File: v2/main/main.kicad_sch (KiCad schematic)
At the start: 90 parts, among them SW1 SW_PUSH, SW10 SW_PUSH, SW11 SW_PUSH, SW12 SW_PUSH, SW13 SW_PUSH, SW14 SW_PUSH, SW15 SW_PUSH, SW16 SW_PUSH, SW17 SW_PUSH, SW18 SW_PUSH, SW19 SW_PUSH, SW2 SW_PUSH, SW20 SW_PUSH, SW21 SW_PUSH, SW22 SW_PUSH, SW23 SW_PUSH, SW24 SW_PUSH, SW25 SW_PUSH, SW26 SW_PUSH, SW27 SW_PUSH, SW28 SW_PUSH, SW29 SW_PUSH, SW3 SW_PUSH, SW30 SW_PUSH, SW31 SW_PUSH, SW32 SW_PUSH, SW33 SW_PUSH, SW34 SW_PUSH, SW35 SW_PUSH, SW36 SW_PUSH, SW37 SW_PUSH, SW38 SW_PUSH, SW39 SW_PUSH, SW4 SW_PUSH, SW40 SW_PUSH, SW41 SW_PUSH, SW42 SW_PUSH, SW43 SW_PUSH, SW44 SW_PUSH, SW45 SW_PUSH, SW5 SW_PUSH, SW6 SW_PUSH, SW7 SW_PUSH, SW8 SW_PUSH, SW9 SW_PUSH

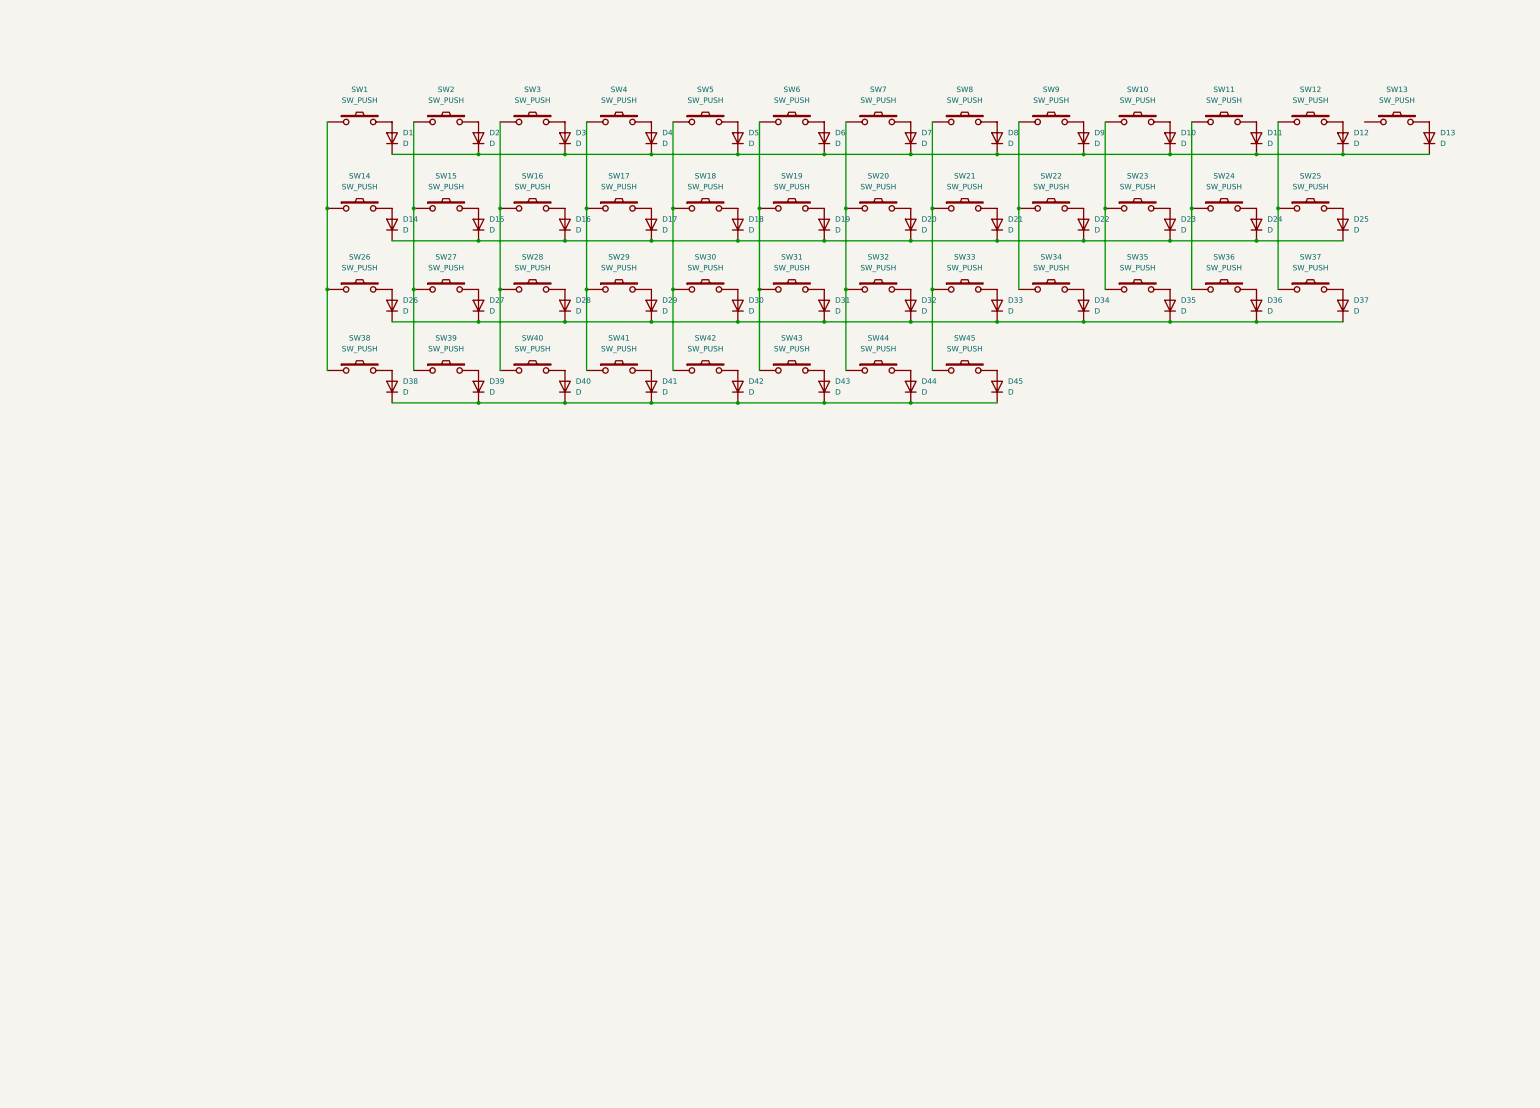
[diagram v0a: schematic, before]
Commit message: Add initial KiCad project files for version 2
- Created top.kicad_pro with board design settings, rules, and dimensions.
- Added top.kicad_sch with basic schematic structure and metadata.
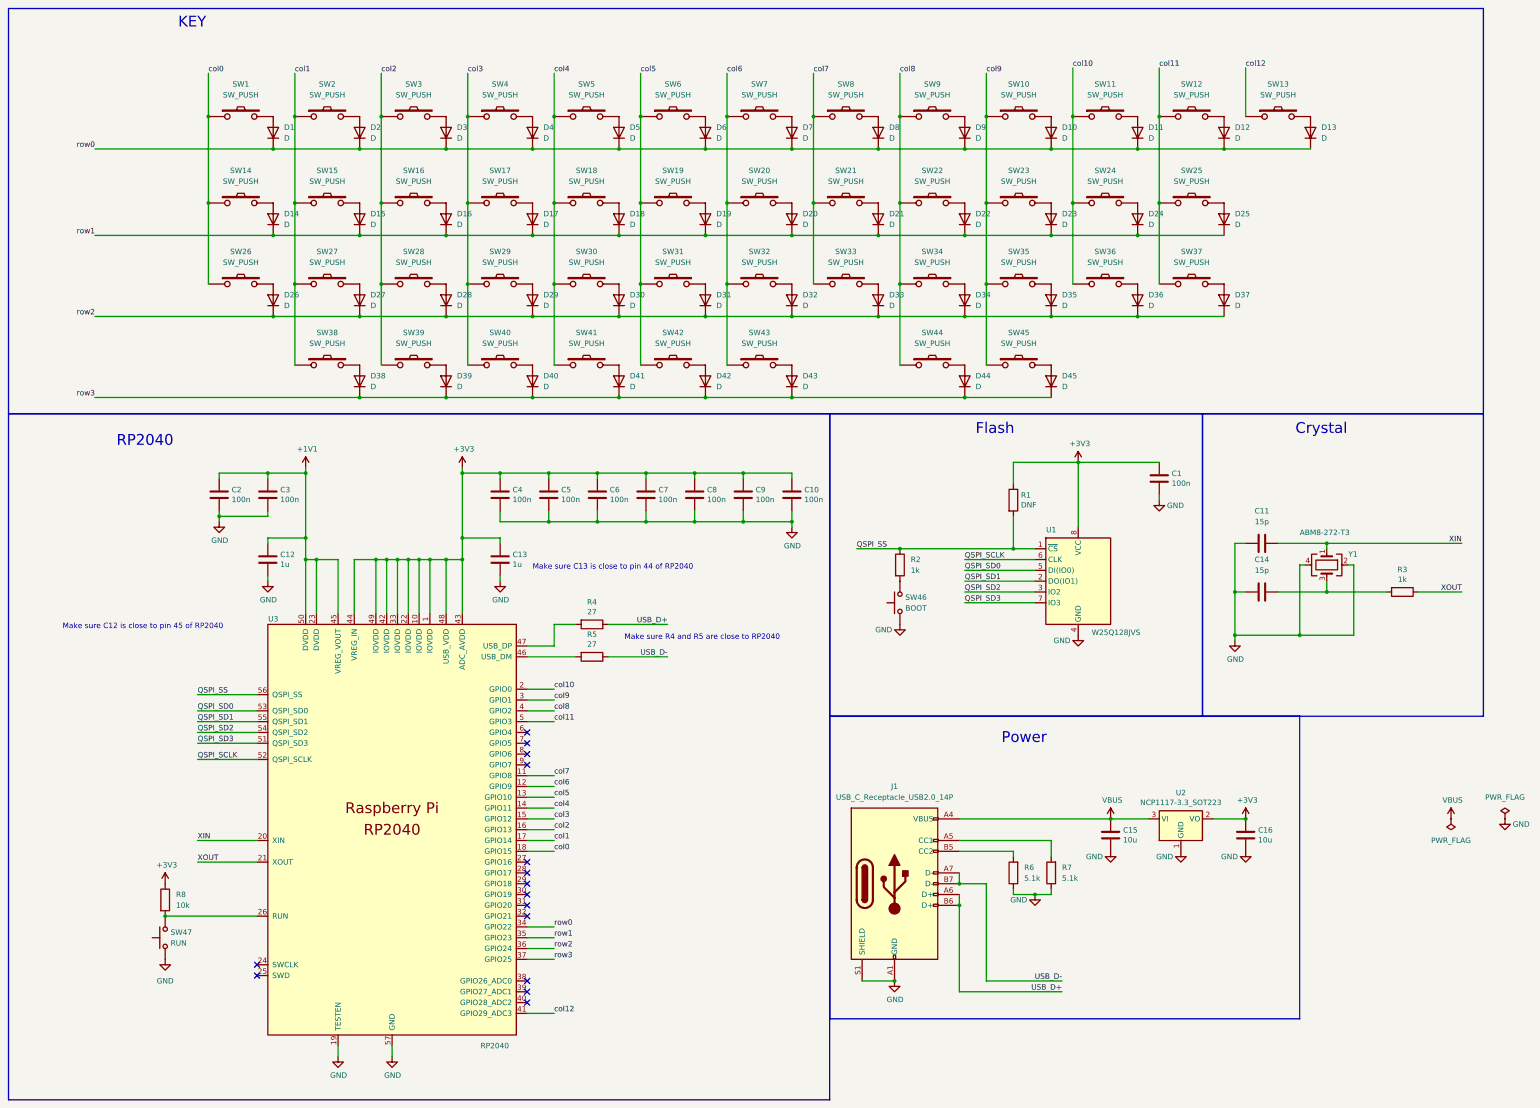
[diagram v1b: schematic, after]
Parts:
- added C1, C10, C2, C3, C4, C5, C6, C7, C8, C9: 100n, Capacitor_SMD:C_0402_1005Metric, symbol Device:C
- added C11, C14: 15p, Capacitor_SMD:C_0603_1608Metric, symbol Device:C
- added C12, C13: 1u, Capacitor_SMD:C_0402_1005Metric, symbol Device:C
- added C15, C16: 10u, Capacitor_SMD:C_0805_2012Metric, symbol Device:C
- added J1: USB_C_Receptacle_USB2.0_14P, Connector_USB:USB_C_Receptacle_Palconn_UTC16-G, symbol Connector:USB_C_Receptacle_USB2.0_14P
- added R1: DNF, Resistor_SMD:R_0402_1005Metric, symbol Device:R
- added R2, R3: 1k, Resistor_SMD:R_0402_1005Metric, symbol Device:R
- added R4, R5: 27, Resistor_SMD:R_0603_1608Metric, symbol Device:R
- added R6, R7: 5.1k, Resistor_SMD:R_0402_1005Metric, symbol Device:R
- added R8: 10k, Resistor_SMD:R_0402_1005Metric, symbol Device:R
- added SW46: BOOT, kamo3_footprint:Tact_Switch_5.1_5.1mm_SMD, symbol kamo3_symbol:SW_Push_4pin
- added SW47: RUN, kamo3_footprint:Tact_Switch_5.1_5.1mm_SMD, symbol kamo3_symbol:SW_Push_4pin
- added U1: W25Q128JVS, Package_SO:SOIC-8_5.23x5.23mm_P1.27mm, symbol Memory_Flash:W25Q128JVS
- added U2: NCP1117-3.3_SOT223, Package_TO_SOT_SMD:SOT-223-3_TabPin2, symbol Regulator_Linear:NCP1117-3.3_SOT223
- added U3: RP2040, rp2040:RP2040-QFN-56, symbol rp2040:RP2040
- added Y1: ABM8-272-T3, Crystal:Crystal_SMD_3225-4Pin_3.2x2.5mm, symbol Device:Crystal_GND24
- D1, D10, D11, D12, D13, D14, D15, D16, D17, D18, D19, D2, D20, D21, D22, D23, D24, D25, D26, D27, D28, D29, D3, D30, D31, D32, D33, D34, D35, D36, D37, D38, D39, D4, D40, D41, D42, D43, D44, D45, D5, D6, D7, D8, D9: LCSC (none) -> C8598
- SW41: footprint kamo3_footprint:SW_CherryMX_Hotswap_2.25u -> kamo3_footprint:SW_CherryMX_Hotswap_1.00u
- SW42: footprint kamo3_footprint:SW_CherryMX_Hotswap_2.75u -> kamo3_footprint:SW_CherryMX_Hotswap_1.00u
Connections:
- net col11: now reaches SW12.1, SW25.1, SW37.1
- net col11: now also U3.5 (GPIO3)
- net row1: now reaches D14.1 (K), D15.1 (K), D16.1 (K), D17.1 (K), D18.1 (K), D19.1 (K), D20.1 (K), D21.1 (K), D22.1 (K), D23.1 (K), D24.1 (K), D25.1 (K)
- net row1: now also U3.35 (GPIO23)
- net row3: now reaches D38.1 (K), D39.1 (K), D40.1 (K), D41.1 (K), D42.1 (K), D43.1 (K), D44.1 (K), D45.1 (K)
- net row3: now also U3.37 (GPIO25)
- net col1: now reaches SW15.1, SW2.1, SW27.1
- net col1: now also SW38.1, U3.17 (GPIO14); no longer SW39.1
- net col5: now reaches SW19.1, SW31.1, SW6.1
- net col5: now also SW42.1, U3.13 (GPIO10); no longer SW43.1
- net col6: now reaches SW20.1, SW32.1, SW7.1
- net col6: now also SW43.1, U3.12 (GPIO9); no longer SW44.1
- net row2: now reaches D26.1 (K), D27.1 (K), D28.1 (K), D29.1 (K), D30.1 (K), D31.1 (K), D32.1 (K), D33.1 (K), D34.1 (K), D35.1 (K), D36.1 (K), D37.1 (K)
- net row2: now also U3.36 (GPIO24)
- net col4: now reaches SW18.1, SW30.1, SW5.1
- net col4: now also SW41.1, U3.14 (GPIO11); no longer SW42.1
- net row0: now reaches D1.1 (K), D10.1 (K), D11.1 (K), D12.1 (K), D13.1 (K), D2.1 (K), D3.1 (K), D4.1 (K), D5.1 (K), D6.1 (K), D7.1 (K), D8.1 (K), D9.1 (K)
- net row0: now also U3.34 (GPIO22)
- net col2: now reaches SW16.1, SW28.1, SW3.1
- net col2: now also SW39.1, U3.16 (GPIO13); no longer SW40.1
- net col3: now reaches SW17.1, SW29.1, SW4.1
- net col3: now also SW40.1, U3.15 (GPIO12); no longer SW41.1
- net col0: now reaches SW1.1, SW14.1, SW26.1
- net col0: now also U3.18 (GPIO15); no longer SW38.1
- net col9: now reaches SW10.1, SW23.1, SW35.1
- net col9: now also SW45.1, U3.3 (GPIO1)
- net col8: now reaches SW22.1, SW34.1, SW9.1
- net col8: now also SW44.1, U3.4 (GPIO2)
- net col7: now reaches SW21.1, SW33.1, SW8.1
- net col7: now also U3.11 (GPIO8); no longer SW45.1
- net col10: now reaches SW11.1, SW24.1, SW36.1
- net col10: now also U3.2 (GPIO0)
- net col12: now reaches SW13.1
- net col12: now also U3.41 (GPIO29_ADC3)
- new net: C14.2, R3.2, Y1.3
- new net: R5.2, U3.46 (USB_DM)
- new net: R8.2, SW47.3, SW47.4, U3.26 (RUN)
- new net: J1.B5 (CC2), R6.2
- new net: R2.2, SW46.3, SW46.4
- new net: R4.2, U3.47 (USB_DP)
- new net: J1.A5 (CC1), R7.2
- new net +1V1: C12.1, C2.1, C3.1, U3.23 (DVDD), U3.45 (VREG_VOUT), U3.50 (DVDD)
- new net +3V3: C1.1, C10.1, C13.1, C16.1, C4.1, C5.1, C6.1, C7.1, C8.1, C9.1, R1.1, R8.1, U1.8 (VCC), U2.2 (VO), U3.1 (IOVDD), U3.10 (IOVDD), U3.22 (IOVDD), U3.33 (IOVDD), U3.42 (IOVDD), U3.43 (ADC_AVDD), U3.44 (VREG_IN), U3.48 (USB_VDD), U3.49 (IOVDD)
- new net GND: C1.2, C10.2, C11.1, C12.2, C13.2, C14.1, C15.2, C16.2, C2.2, C3.2, C4.2, C5.2, C6.2, C7.2, C8.2, C9.2, J1.A1 (GND), J1.A12 (GND), J1.B1 (GND), J1.B12 (GND), J1.S1 (SHIELD), R6.1, R7.1, SW46.1, SW46.2, SW47.1, SW47.2, U1.4 (GND), U2.1 (GND), U3.19 (TESTEN), U3.57 (GND), Y1.2, Y1.4
- new net QSPI_SCLK: U1.6 (CLK), U3.52 (QSPI_SCLK)
- new net QSPI_SD0: U1.5 (DI(IO0)), U3.53 (QSPI_SD0)
- new net QSPI_SD1: U1.2 (DO(IO1)), U3.55 (QSPI_SD1)
- new net QSPI_SD2: U1.3 (IO2), U3.54 (QSPI_SD2)
- new net QSPI_SD3: U1.7 (IO3), U3.51 (QSPI_SD3)
- new net QSPI_SS: R1.2, R2.1, U1.1 (~{CS}), U3.56 (QSPI_SS)
- new net USB_D+: J1.A6 (D+), J1.B6 (D+), R4.1
- new net USB_D-: J1.A7 (D-), J1.B7 (D-), R5.1
- new net VBUS: C15.1, J1.A4 (VBUS), J1.A9 (VBUS), J1.B4 (VBUS), J1.B9 (VBUS), U2.3 (VI)
- new net XIN: C11.2, U3.20 (XIN), Y1.1
- new net XOUT: R3.1, U3.21 (XOUT)
- no-connect marks 0 -> 15
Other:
- note added: "Crystal"
- note added: "Flash"
- note added: "KEY"
- note added: "Make sure C12 is close to pin 45 of RP2040"
- note added: "Make sure C13 is close to pin 44 of RP2040"
- note added: "Make sure R4 and R5 are close to RP2040"
- note added: "Power"
- note added: "RP2040"
- moved on the sheet: D1, D10, D11, D12, D13, D14, D15, D16, D17, D18, D19, D2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
